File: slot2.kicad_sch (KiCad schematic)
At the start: 1 part

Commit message: board layout
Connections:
- net AD1: now also PL2.a3 (Pin_a3); no longer PL2.b3 (Pin_b3)
- net Chroma: now also PL2.a2 (Pin_a2); no longer PL2.b2 (Pin_b2)
- net GND: now also PL2.b3 (Pin_b3); no longer PL2.a3 (Pin_a3)
- net Luma: now also PL2.b2 (Pin_b2); no longer PL2.a2 (Pin_a2)
- net VCLK: now reaches PL2.a38 (Pin_a38)
- net ESND: now reaches PL2.b10 (Pin_b10)
- no-connect marks 1 -> 0
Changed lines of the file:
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@@
 	(generator_version "8.0")
 	(paper "A4")
-	(no_connect
-		(at 114.3 74.93)
-	)
 	(global_label "AD1"
 		(shape bidirectional)
-		(at 114.3 57.15 0)
+		(at 101.6 57.15 180)
 		(fields_autoplaced yes)
 		(effects
@@
 				(size 1.27 1.27)
 			)
-			(justify left)
+			(justify right)
 		)
 		(property "Intersheetrefs" "${INTERSHEET_REFS}"
-			(at 121.9646 57.15 0)
+			(at 93.9354 57.15 0)
 			(effects
 				(font
 					(size 1.27 1.27)
 				)
-				(justify left)
+				(justify right)
 				(hide yes)
 			)
@@
 	(global_label "Luma"
 		(shape bidirectional)
-		(at 101.6 54.61 180)
+		(at 114.3 54.61 0)
 		(fields_autoplaced yes)
 		(effects
@@
 				(size 1.27 1.27)
 			)
-			(justify right)
+			(justify left)
 		)
 		(property "Intersheetrefs" "${INTERSHEET_REFS}"
-			(at 92.4841 54.61 0)
+			(at 123.4159 54.61 0)
 			(effects
 				(font
 					(size 1.27 1.27)
 				)
-				(justify right)
+				(justify left)
 				(hide yes)
 			)
@@
 		)
 	)
+	(global_label "VCLK"
+		(shape bidirectional)
+		(at 101.6 146.05 180)
+		(fields_autoplaced yes)
+		(effects
+			(font
+				(size 1.27 1.27)
+			)
+			(justify right)
+		)
+		(property "Intersheetrefs" "${INTERSHEET_REFS}"
+			(at 92.8468 146.05 0)
+			(effects
+				(font
+					(size 1.27 1.27)
+				)
+				(justify right)
+				(hide yes)
+			)
+		)
+	)
 	(global_label "A14"
 		(shape bidirectional)
@@
 	(global_label "Chroma"
 		(shape bidirectional)
-		(at 114.3 54.61 0)
+		(at 101.6 54.61 180)
 		(fields_autoplaced yes)
 		(effects
@@
 				(size 1.27 1.27)
 			)
-			(justify left)
+			(justify right)
 		)
 		(property "Intersheetrefs" "${INTERSHEET_REFS}"
-			(at 125.593 54.61 0)
+			(at 90.307 54.61 0)
 			(effects
 				(font
 					(size 1.27 1.27)
 				)
-				(justify left)
+				(justify right)
 				(hide yes)
 			)
@@
 		)
 	)
+	(global_label "ESND"
+		(shape bidirectional)
+		(at 114.3 74.93 0)
+		(fields_autoplaced yes)
+		(effects
+			(font
+				(size 1.27 1.27)
+			)
+			(justify left)
+		)
+		(property "Intersheetrefs" "${INTERSHEET_REFS}"
+			(at 122.2442 74.93 0)
+			(effects
+				(font
+					(size 1.27 1.27)
+				)
+				(justify left)
+				(hide yes)
+			)
+		)
+	)
 	(global_label "R2"
 		(shape bidirectional)
@@
 	(symbol
 		(lib_id "power:GND")
-		(at 101.6 57.15 270)
+		(at 114.3 57.15 90)
+		(mirror x)
 		(unit 1)
 		(exclude_from_sim no)
@@
 		(fields_autoplaced yes)
 		(property "Reference" "#PWR05"
-			(at 95.25 57.15 0)
+			(at 120.65 57.15 0)
 			(effects
 				(font
@@
 		)
 		(property "Value" "GND"
-			(at 97.79 57.1499 90)
+			(at 118.11 57.1499 90)
 			(effects
 				(font
@@
 		)
 		(property "Footprint" ""
-			(at 101.6 57.15 0)
+			(at 114.3 57.15 0)
 			(effects
 				(font
@@
 		)
 		(property "Datasheet" ""
-			(at 101.6 57.15 0)
+			(at 114.3 57.15 0)
 			(effects
 				(font
@@
 		)
 		(property "Description" "Power symbol creates a global label with name \"GND\" , ground"
-			(at 101.6 57.15 0)
+			(at 114.3 57.15 0)
 			(effects
 				(font

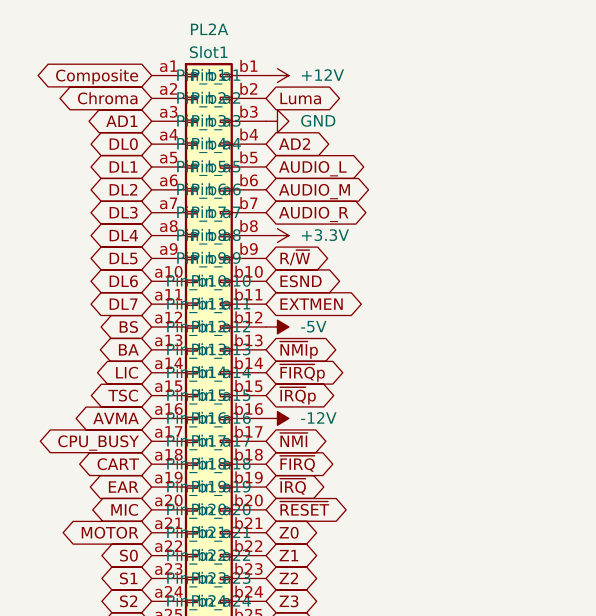
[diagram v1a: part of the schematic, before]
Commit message: revise bus tracing
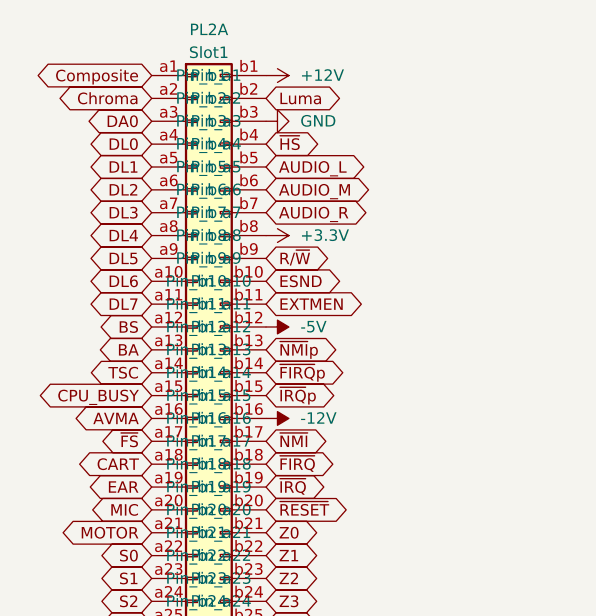
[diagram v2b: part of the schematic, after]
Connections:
- net LIC is gone; now on net TSC: PL2.a14 (Pin_a14)
- net CPU_BUSY: now also PL2.a15 (Pin_a15); no longer PL2.a17 (Pin_a17)
- net TSC: no longer PL2.a15 (Pin_a15)
- net AD1 renamed DA0
- net AD2 renamed ~{HS}
- new net ~{FS}: PL2.a17 (Pin_a17)
